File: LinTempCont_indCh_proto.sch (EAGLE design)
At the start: 26 parts

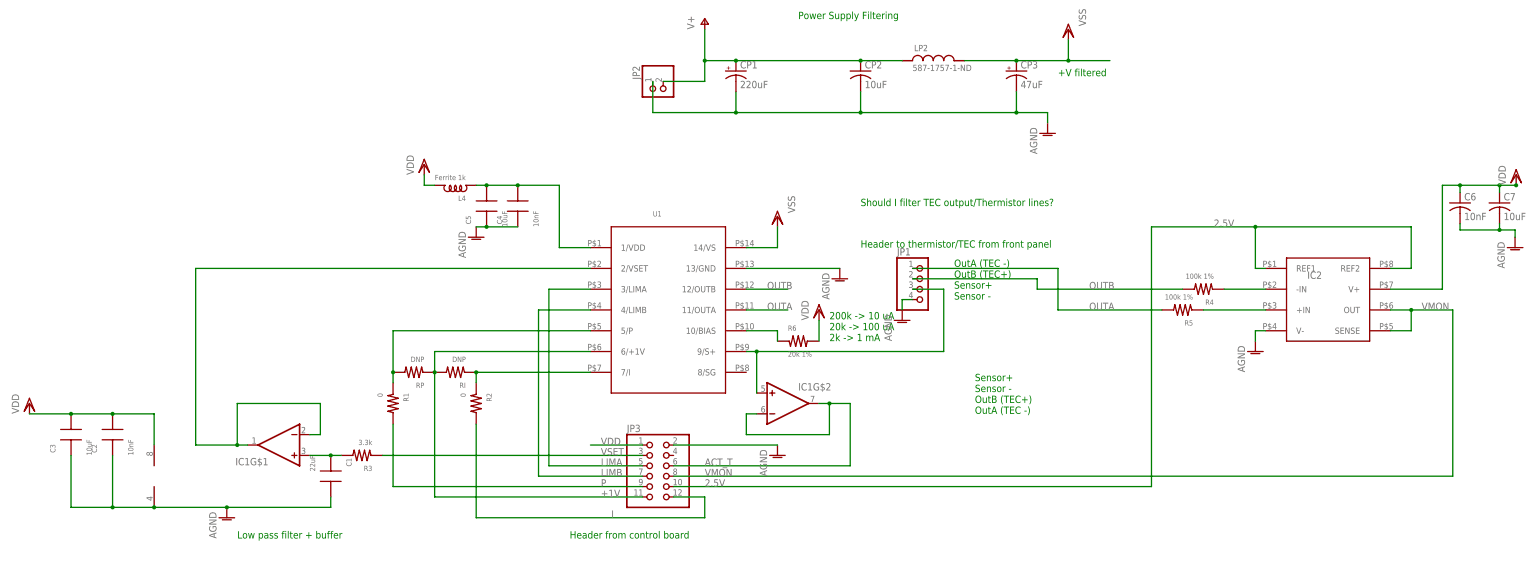
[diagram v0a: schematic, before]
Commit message: Schematic updates and progress routing both boards
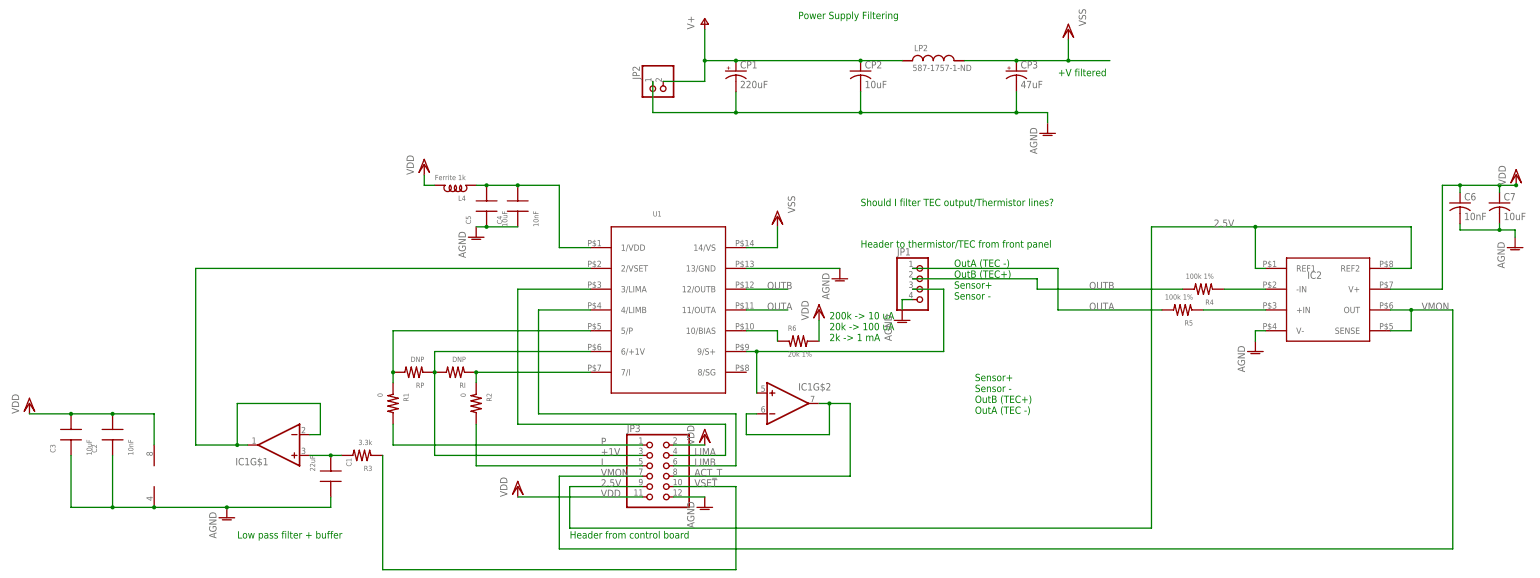
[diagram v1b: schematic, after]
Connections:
- net +1V: now also JP3.3; no longer JP3.11
- net 2.5V: now also JP3.9; no longer JP3.10
- net ACT_T: now also JP3.8; no longer JP3.6
- net AGND: now also JP3.12; no longer JP3.2
- net I: now also JP3.5; no longer JP3.12
- net LIMA: now also JP3.4; no longer JP3.5
- net LIMB: now also JP3.6; no longer JP3.7
- net P: now also JP3.1; no longer JP3.9
- net VDD: now also JP3.11, JP3.2; no longer JP3.1
- net VMON: now also JP3.7; no longer JP3.8
- net VSET: now also JP3.10; no longer JP3.3

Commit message: Board/Schematic updates and tweaks
Incorporate suggestions from Neal and Alessandro
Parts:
- added C8: 100nF, rlc-jqi:CAP0603
- added RSG: DNP, rlc-jqi:RES0603
- R6: device rlc-jqi:RES0603 -> jqi_passives:R_SMDR0805
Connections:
- new net N$6: RSG.P$2, U1.8/SG
- net AGND: now also C8.P$1, RSG.P$1
- net N$2: now also C8.P$2
- net N$4: now also R6.1; no longer R6.P$1
- net VDD: now also R6.2; no longer R6.P$2
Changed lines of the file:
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@@
 <part name="C3" library="rlc-jqi" deviceset="CAP" device="0603" value="10uF"/>
 <part name="VDD1" library="supply1" deviceset="VDD" device=""/>
-<part name="R6" library="rlc-jqi" deviceset="RES" device="0603" value="20k 1%"/>
+<part name="R6" library="jqi_passives" deviceset="R_SMD" device="R0805" value="20k 1%"/>
 <part name="VDD2" library="supply1" deviceset="VDD" device=""/>
 <part name="AGND5" library="supply1" deviceset="AGND" device=""/>
@@
 <part name="VDD3" library="supply1" deviceset="VDD" device=""/>
 <part name="VDD4" library="supply1" deviceset="VDD" device=""/>
+<part name="C8" library="rlc-jqi" deviceset="CAP" device="0603" value="100nF"/>
+<part name="AGND1" library="supply1" deviceset="AGND" device=""/>
+<part name="RSG" library="rlc-jqi" deviceset="RES" device="0603" value="DNP"/>
 </parts>
 <sheets>
@@
 <instance part="VDD3" gate="G$1" x="-5.08" y="-45.72"/>
 <instance part="VDD4" gate="G$1" x="40.64" y="-33.02"/>
+<instance part="C8" gate="G$1" x="91.44" y="-17.78" rot="R90"/>
+<instance part="AGND1" gate="VR1" x="91.44" y="-27.94"/>
+<instance part="RSG" gate="G$1" x="71.12" y="-17.78" rot="R180"/>
 </instances>
 <busses>
@@
 <pinref part="AGND6" gate="VR1" pin="AGND"/>
 </segment>
+<segment>
+<pinref part="C8" gate="G$1" pin="P$1"/>
+<pinref part="AGND1" gate="VR1" pin="AGND"/>
+<wire x1="91.44" y1="-25.4" x2="91.44" y2="-22.86" width="0.1524" layer="91"/>
+<pinref part="RSG" gate="G$1" pin="P$1"/>
+<wire x1="76.2" y1="-17.78" x2="83.82" y2="-17.78" width="0.1524" layer="91"/>
+<wire x1="83.82" y1="-17.78" x2="83.82" y2="-22.86" width="0.1524" layer="91"/>
+<wire x1="83.82" y1="-22.86" x2="91.44" y2="-22.86" width="0.1524" layer="91"/>
+<junction x="91.44" y="-22.86"/>
+</segment>
 </net>
 <net name="VDD" class="0">
@@
 </segment>
 <segment>
-<pinref part="R6" gate="G$1" pin="P$2"/>
+<pinref part="R6" gate="G$1" pin="2"/>
 <pinref part="VDD2" gate="G$1" pin="VDD"/>
 <wire x1="68.58" y1="-10.16" x2="68.58" y2="-5.08" width="0.1524" layer="91"/>
@@
 <segment>
 <pinref part="U1" gate="G$1" pin="9/S+"/>
-<wire x1="99.06" y1="-12.7" x2="53.34" y2="-12.7" width="0.1524" layer="91"/>
+<wire x1="99.06" y1="-12.7" x2="91.44" y2="-12.7" width="0.1524" layer="91"/>
 <pinref part="IC1" gate="G$2" pin="+IN"/>
+<wire x1="91.44" y1="-12.7" x2="53.34" y2="-12.7" width="0.1524" layer="91"/>
 <wire x1="53.34" y1="-12.7" x2="50.8" y2="-12.7" width="0.1524" layer="91"/>
 <wire x1="53.34" y1="-22.86" x2="53.34" y2="-12.7" width="0.1524" layer="91"/>
@@
 <pinref part="JP1" gate="A" pin="3"/>
 <junction x="53.34" y="-12.7"/>
+<pinref part="C8" gate="G$1" pin="P$2"/>
+<junction x="91.44" y="-12.7"/>
 </segment>
 </net>
@@
 <net name="N$4" class="0">
 <segment>
-<pinref part="R6" gate="G$1" pin="P$1"/>
+<pinref part="R6" gate="G$1" pin="1"/>
 <wire x1="58.42" y1="-10.16" x2="58.42" y2="-7.62" width="0.1524" layer="91"/>
 <pinref part="U1" gate="G$1" pin="10/BIAS"/>
@@
 </segment>
 </net>
+<net name="N$6" class="0">
+<segment>
+<pinref part="U1" gate="G$1" pin="8/SG"/>
+<pinref part="RSG" gate="G$1" pin="P$2"/>
+<wire x1="66.04" y1="-17.78" x2="50.8" y2="-17.78" width="0.1524" layer="91"/>
+</segment>
+</net>

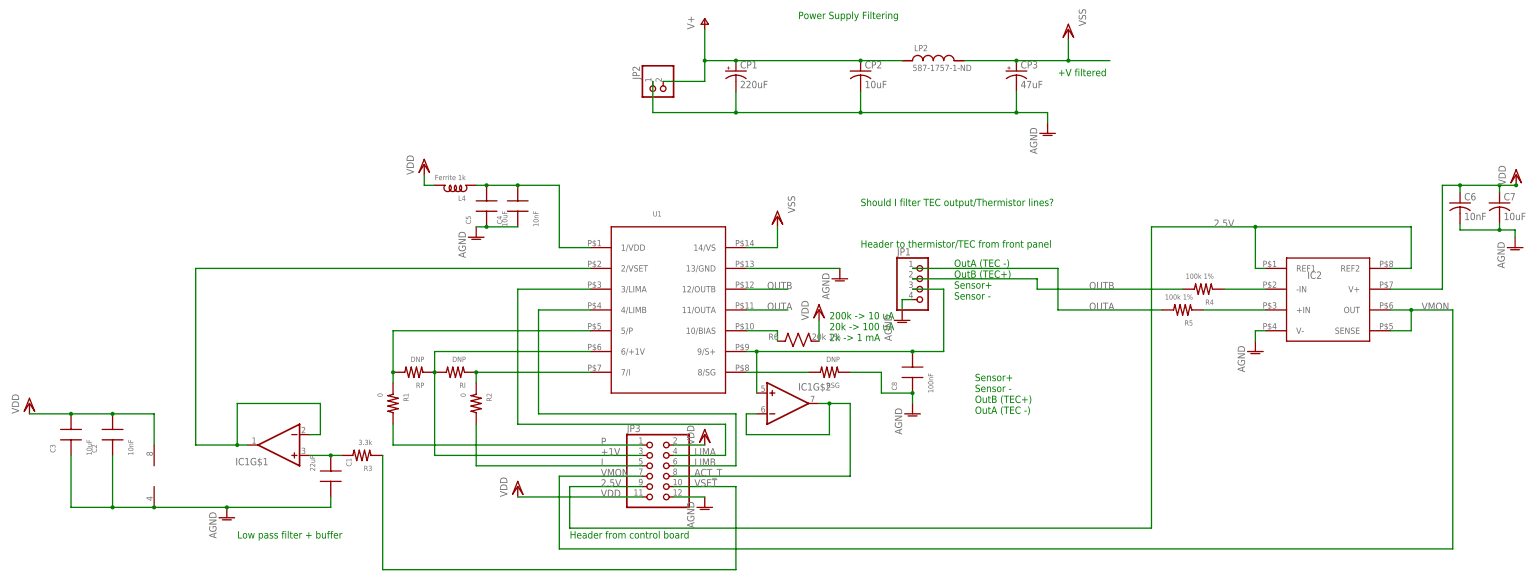
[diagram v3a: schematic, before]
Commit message: Add BOM, minor updates to reflect part availability
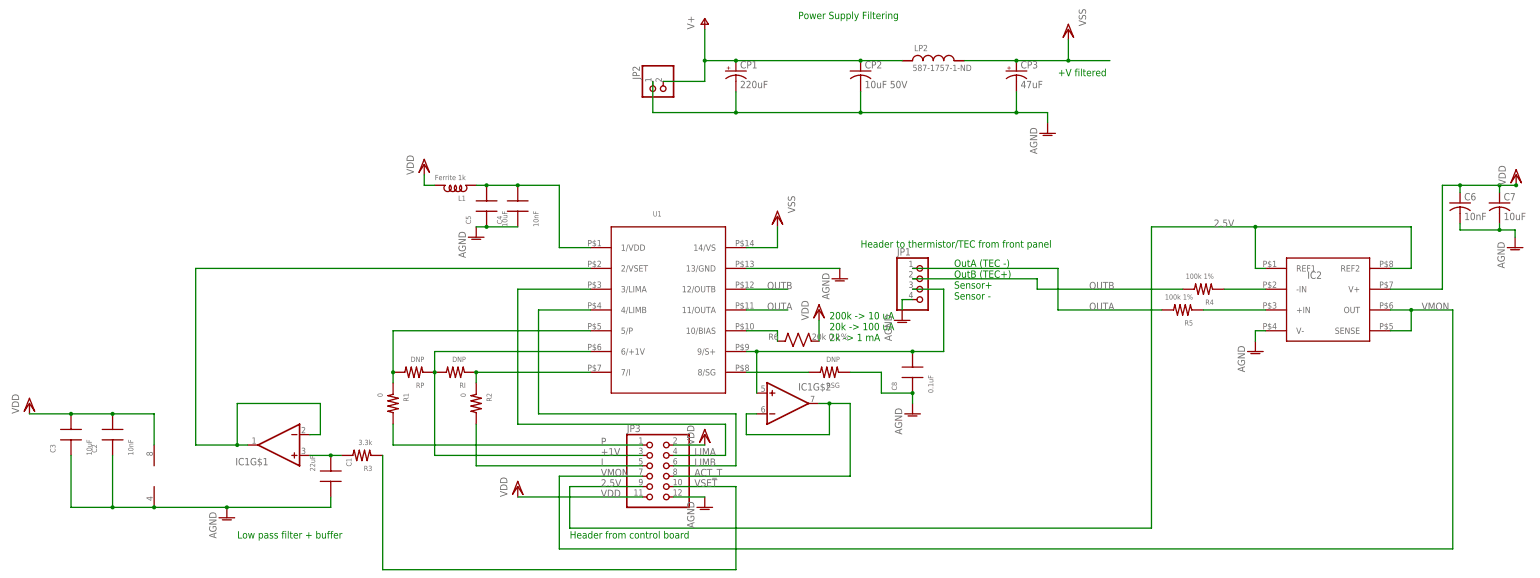
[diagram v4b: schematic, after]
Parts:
- C3, C4: device rlc-jqi:CAP0603 -> rlc-jqi:CAP0805
- C7: device rcl:C-USC0603 -> rcl:C-USC0805
- C8: value 100nF -> 0.1uF
- CP2: value 10uF -> 10uF 50V; device rcl:C-USC0805K -> rcl:C-USC1206
- JP1: device Lin-Temp-Controller:SCRWTRM-1X4/90 -> Lin-Temp-Controller:SCRWTRM-1X4/90_ED550
- JP2: device Lin-Temp-Controller:SCRWTRM-1X2/90 -> Lin-Temp-Controller:SCRWTRM-1X2/90_ED550
- R6: value 20k 1% -> 20k 0.1%
- renumbered L4 to L1
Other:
- note removed: "Sensor+ Sensor - OutB (TEC+) OutA (TEC -)"
- note removed: "Should I filter TEC output/Thermistor lines?"
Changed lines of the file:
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@@
 <parts>
 <part name="U1" library="Lin-Temp-Controller" deviceset="WTC3243" device=""/>
-<part name="JP1" library="Lin-Temp-Controller" deviceset="SCRWTRM-1X4" device="/90"/>
-<part name="JP2" library="Lin-Temp-Controller" deviceset="SCRWTRM-1X2" device="/90"/>
+<part name="JP1" library="Lin-Temp-Controller" deviceset="SCRWTRM-1X4" device="/90_ED550"/>
+<part name="JP2" library="Lin-Temp-Controller" deviceset="SCRWTRM-1X2" device="/90_ED550"/>
 <part name="JP3" library="pinhead" deviceset="PINHD-2X6" device=""/>
-<part name="C4" library="rlc-jqi" deviceset="CAP" device="0603" value="10nF"/>
+<part name="C4" library="rlc-jqi" deviceset="CAP" device="0805" value="10nF"/>
 <part name="C5" library="rlc-jqi" deviceset="CAP" device="0603" value="10uF"/>
 <part name="VDD15" library="supply1" deviceset="VDD" device=""/>
-<part name="L4" library="rlc-jqi" deviceset="INDUCTOR" device="-0805" value="Ferrite 1k"/>
+<part name="L1" library="rlc-jqi" deviceset="INDUCTOR" device="-0805" value="Ferrite 1k"/>
 <part name="AGND25" library="supply1" deviceset="AGND" device=""/>
 <part name="RP" library="rlc-jqi" deviceset="RES" device="0603" value="DNP"/>
@@
 <part name="R4" library="rlc-jqi" deviceset="RES" device="0603" value="100k 1%"/>
 <part name="R5" library="rlc-jqi" deviceset="RES" device="0603" value="100k 1%"/>
-<part name="C7" library="rcl" deviceset="C-US" device="C0603" value="10uF"/>
+<part name="C7" library="rcl" deviceset="C-US" device="C0805" value="10uF"/>
 <part name="C6" library="rcl" deviceset="C-US" device="C0603" value="10nF"/>
 <part name="VDD9" library="supply1" deviceset="VDD" device=""/>
@@
 <part name="CP1" library="rcl" deviceset="CPOL-US" device="F" value="220uF"/>
 <part name="CP3" library="rcl" deviceset="CPOL-US" device="CT7343" value="47uF"/>
-<part name="CP2" library="rcl" deviceset="C-US" device="C0805K" value="10uF"/>
+<part name="CP2" library="rcl" deviceset="C-US" device="C1206" value="10uF 50V"/>
 <part name="LP2" library="jqi_passives" deviceset="L_FERRITE_SMD" device="" value="587-1757-1-ND"/>
 <part name="P+2" library="supply1" deviceset="V+" device=""/>
@@
 <part name="AGND4" library="supply1" deviceset="AGND" device=""/>
 <part name="C2" library="rlc-jqi" deviceset="CAP" device="0603" value="10nF"/>
-<part name="C3" library="rlc-jqi" deviceset="CAP" device="0603" value="10uF"/>
+<part name="C3" library="rlc-jqi" deviceset="CAP" device="0805" value="10uF"/>
 <part name="VDD1" library="supply1" deviceset="VDD" device=""/>
-<part name="R6" library="jqi_passives" deviceset="R_SMD" device="R0805" value="20k 1%"/>
+<part name="R6" library="jqi_passives" deviceset="R_SMD" device="R0805" value="20k 0.1%"/>
 <part name="VDD2" library="supply1" deviceset="VDD" device=""/>
 <part name="AGND5" library="supply1" deviceset="AGND" device=""/>
@@
 <part name="VDD3" library="supply1" deviceset="VDD" device=""/>
 <part name="VDD4" library="supply1" deviceset="VDD" device=""/>
-<part name="C8" library="rlc-jqi" deviceset="CAP" device="0603" value="100nF"/>
+<part name="C8" library="rlc-jqi" deviceset="CAP" device="0603" value="0.1uF"/>
 <part name="AGND1" library="supply1" deviceset="AGND" device=""/>
 <part name="RSG" library="rlc-jqi" deviceset="RES" device="0603" value="DNP"/>
@@
 <text x="63.5" y="68.58" size="1.778" layer="91">Power Supply Filtering</text>
 <text x="78.74" y="12.7" size="1.778" layer="91">Header to thermistor/TEC from front panel</text>
-<text x="78.74" y="22.86" size="1.778" layer="91">Should I filter TEC output/Thermistor lines?</text>
-<text x="106.68" y="-27.94" size="1.778" layer="91">Sensor+
-Sensor -
-OutB (TEC+)
-OutA (TEC -)</text>
 <text x="127" y="54.61" size="1.778" layer="91">+V filtered</text>
 <text x="71.12" y="-10.16" size="1.778" layer="91">200k -&gt; 10 uA
@@
 <instance part="C5" gate="G$1" x="-12.7" y="22.86" rot="R90"/>
 <instance part="VDD15" gate="G$1" x="-27.94" y="33.02"/>
-<instance part="L4" gate="G$1" x="-20.32" y="27.94" rot="R180"/>
+<instance part="L1" gate="G$1" x="-20.32" y="27.94" rot="R180"/>
 <instance part="AGND25" gate="VR1" x="-15.24" y="15.24"/>
 <instance part="RP" gate="G$1" x="-30.48" y="-17.78" rot="R180"/>
@@
 <net name="VDD" class="0">
 <segment>
-<pinref part="L4" gate="G$1" pin="P$2"/>
+<pinref part="L1" gate="G$1" pin="P$2"/>
 <wire x1="-25.4" y1="27.94" x2="-27.94" y2="27.94" width="0.1524" layer="91"/>
 <pinref part="VDD15" gate="G$1" pin="VDD"/>
@@
 <wire x1="5.08" y1="27.94" x2="-5.08" y2="27.94" width="0.1524" layer="91"/>
 <junction x="-5.08" y="27.94"/>
-<pinref part="L4" gate="G$1" pin="P$1"/>
+<pinref part="L1" gate="G$1" pin="P$1"/>
 <wire x1="-12.7" y1="27.94" x2="-15.24" y2="27.94" width="0.1524" layer="91"/>
 <junction x="-12.7" y="27.94"/>
